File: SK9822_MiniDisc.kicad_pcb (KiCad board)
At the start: 4 copper layers, 220 x 220 mm, 378 parts, among them P1 CONN_01X04, P2 CONN_01X04

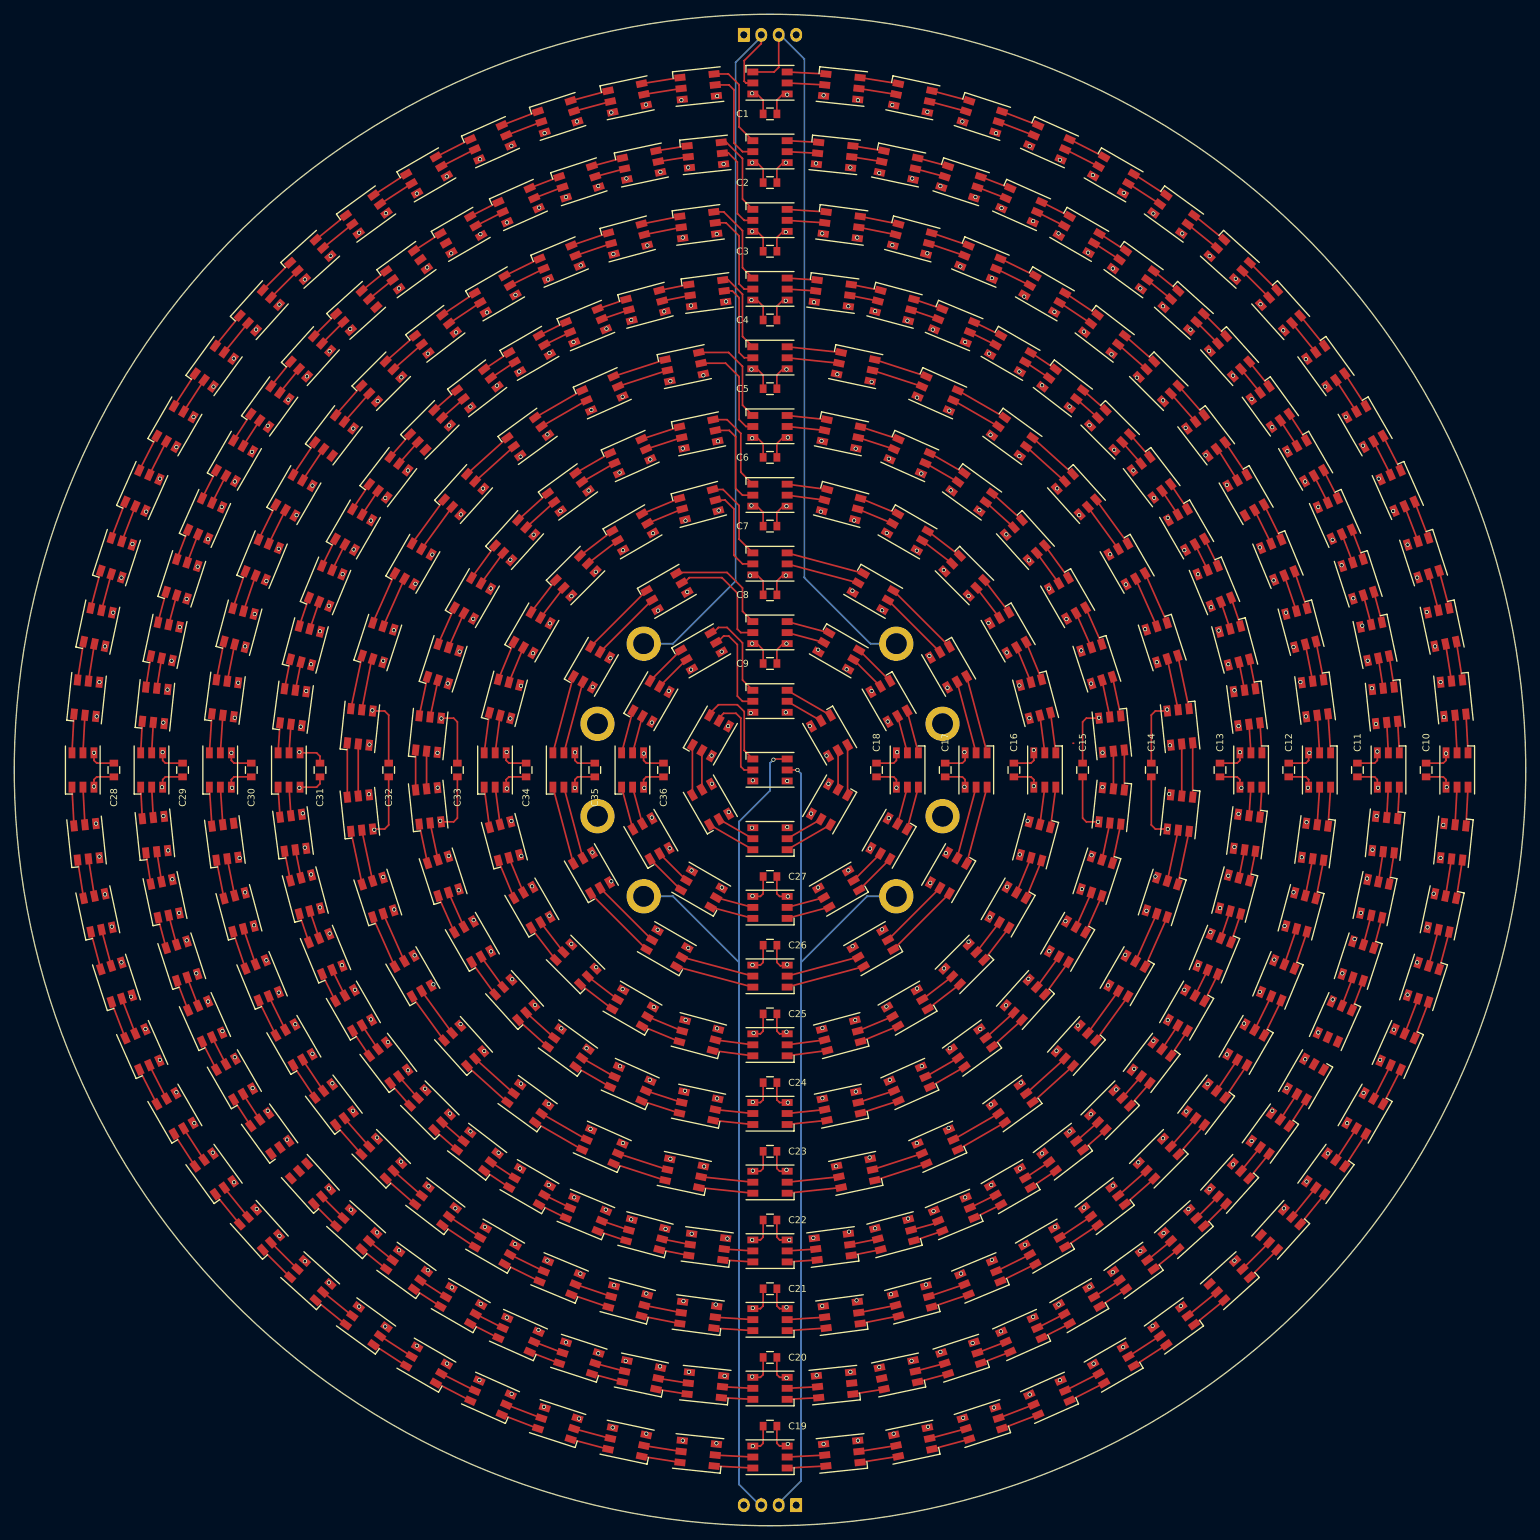
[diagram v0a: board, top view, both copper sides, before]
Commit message: fixing unconnected
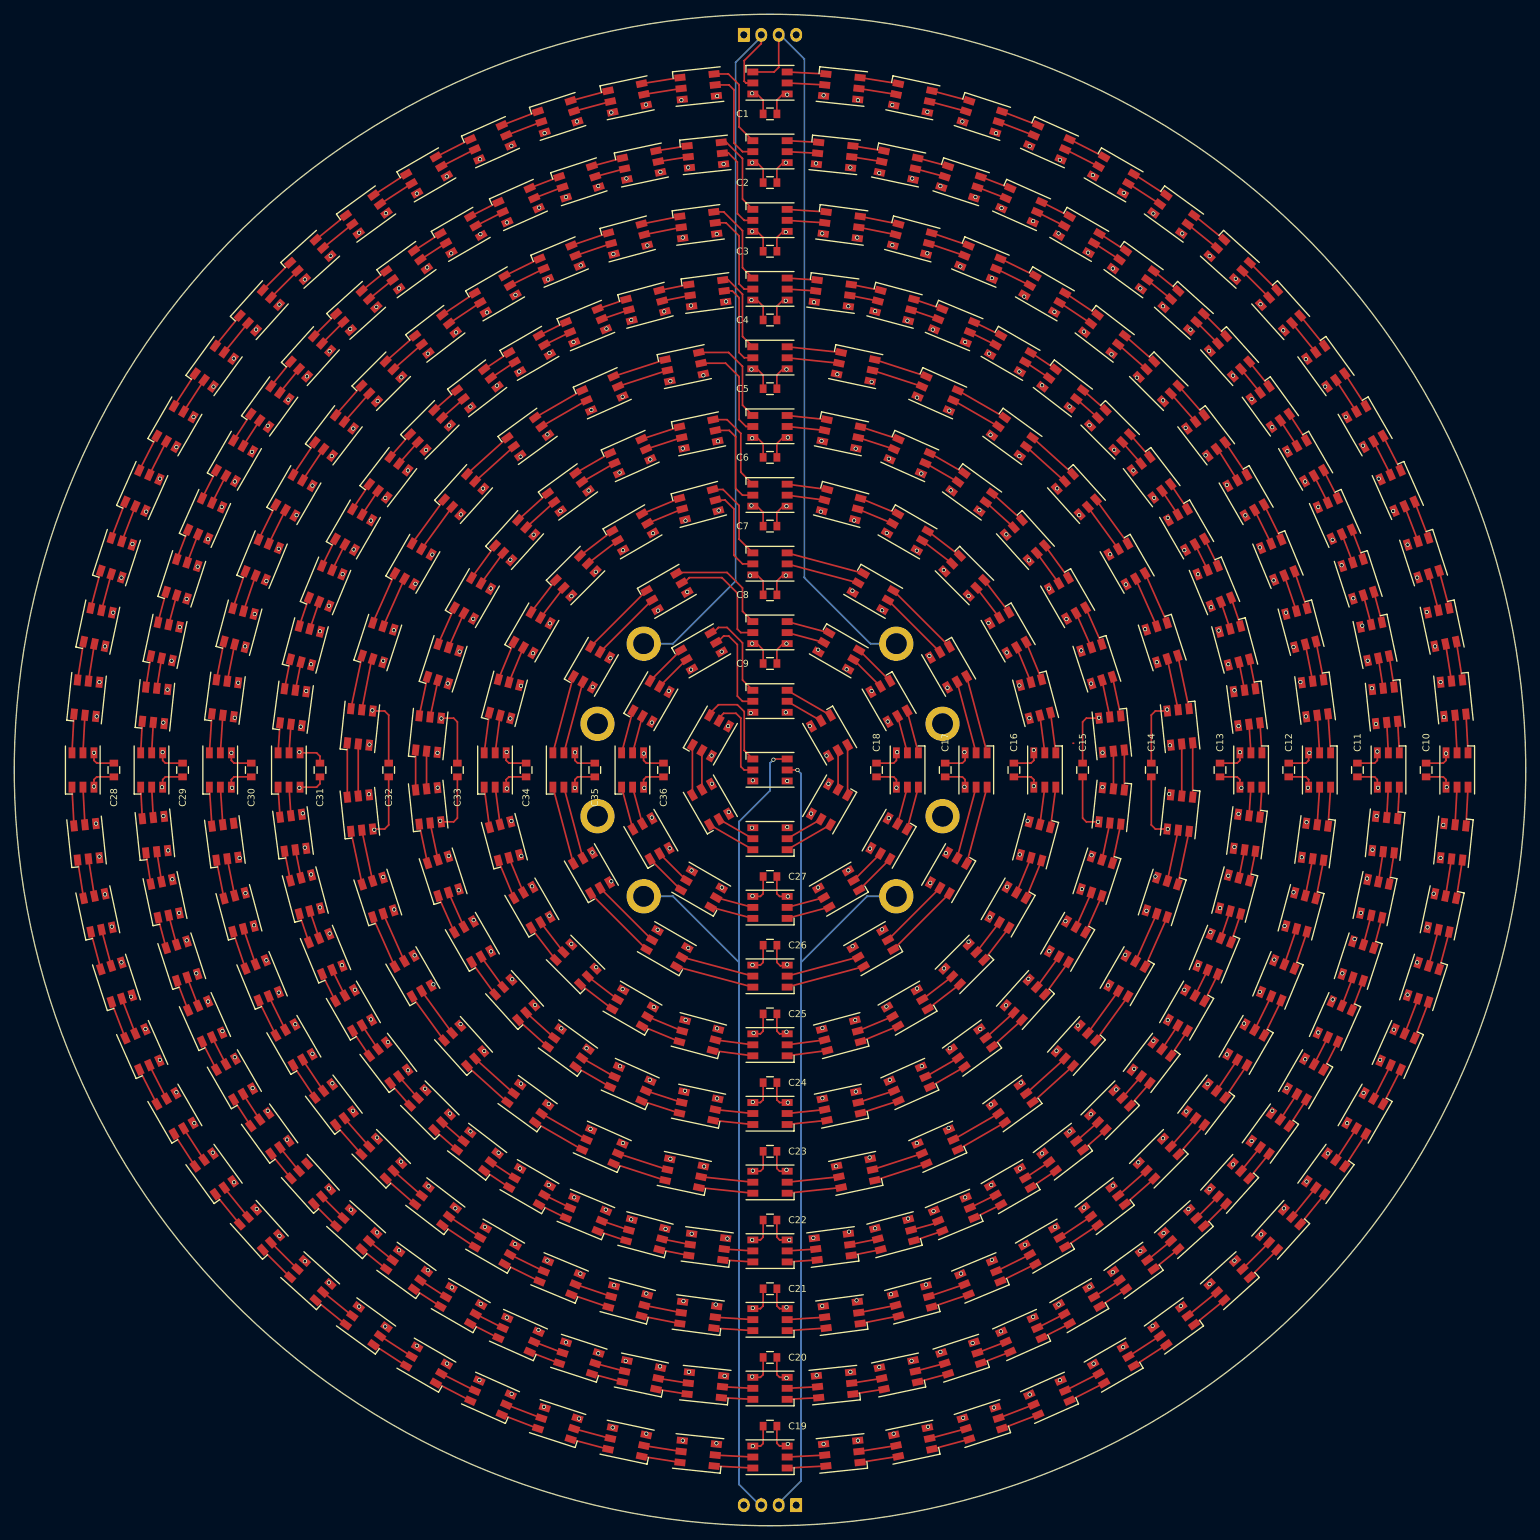
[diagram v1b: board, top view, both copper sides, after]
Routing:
- net VCC: track 4185.0 -> 4203.2 mm, vias 326 -> 330
- net Net-(D100-Pad1): track 0.00 -> 4.59 mm
- net Net-(D80-Pad6): track 0.00 -> 4.59 mm
- net Net-(D115-Pad5): track 0.00 -> 4.43 mm
- net Net-(D100-Pad2): track 0.00 -> 4.43 mm
- net Net-(D89-Pad5): track 0.00 -> 4.43 mm
- net Net-(D80-Pad5): track 0.00 -> 4.43 mm
- net GND: track 4218.6 -> 4218.5 mm, vias 329 -> 331
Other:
- board text added: "CLK_IN"
- board text added: "CLK_OUT"
- board text added: "DAT_IN"
- board text added: "DAT_OUT"
- board text added: "INPUT"
- board text added: "OUTPUT"

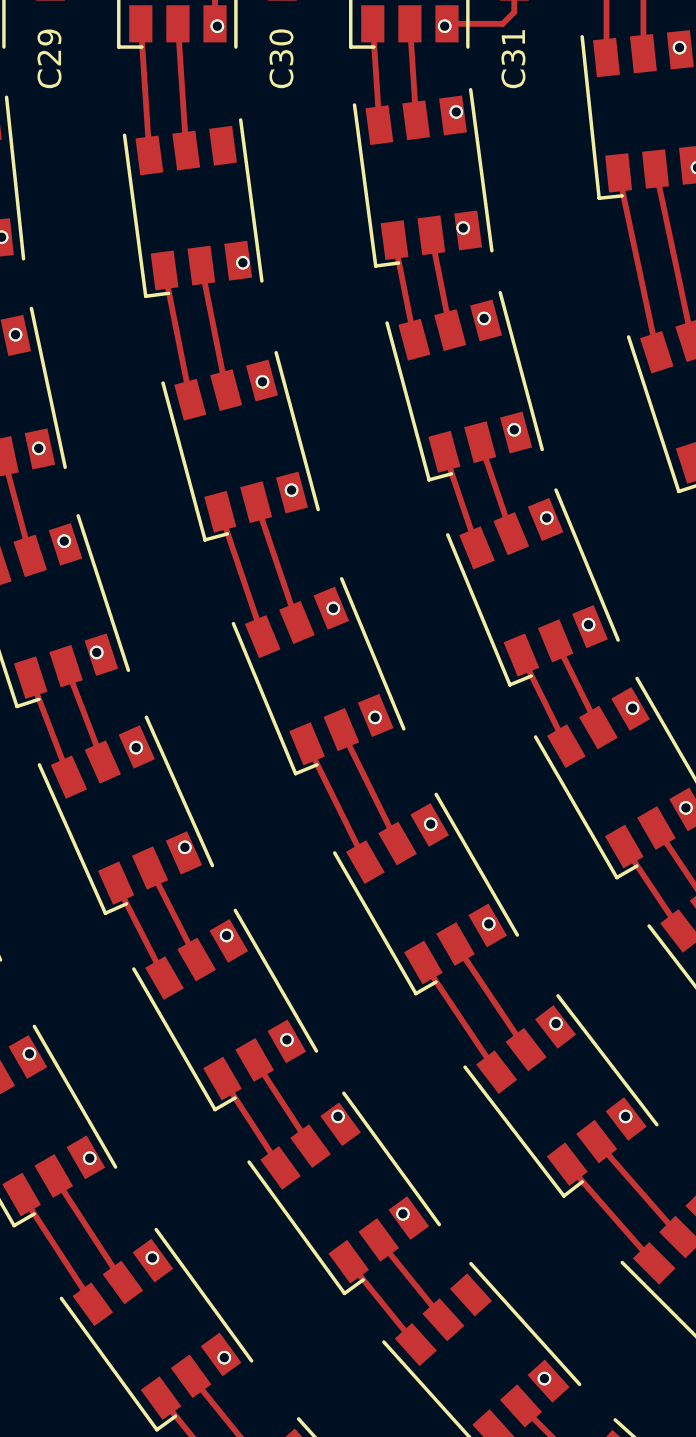
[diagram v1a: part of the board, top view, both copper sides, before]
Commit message: Added vias to D99 and D156 VCC
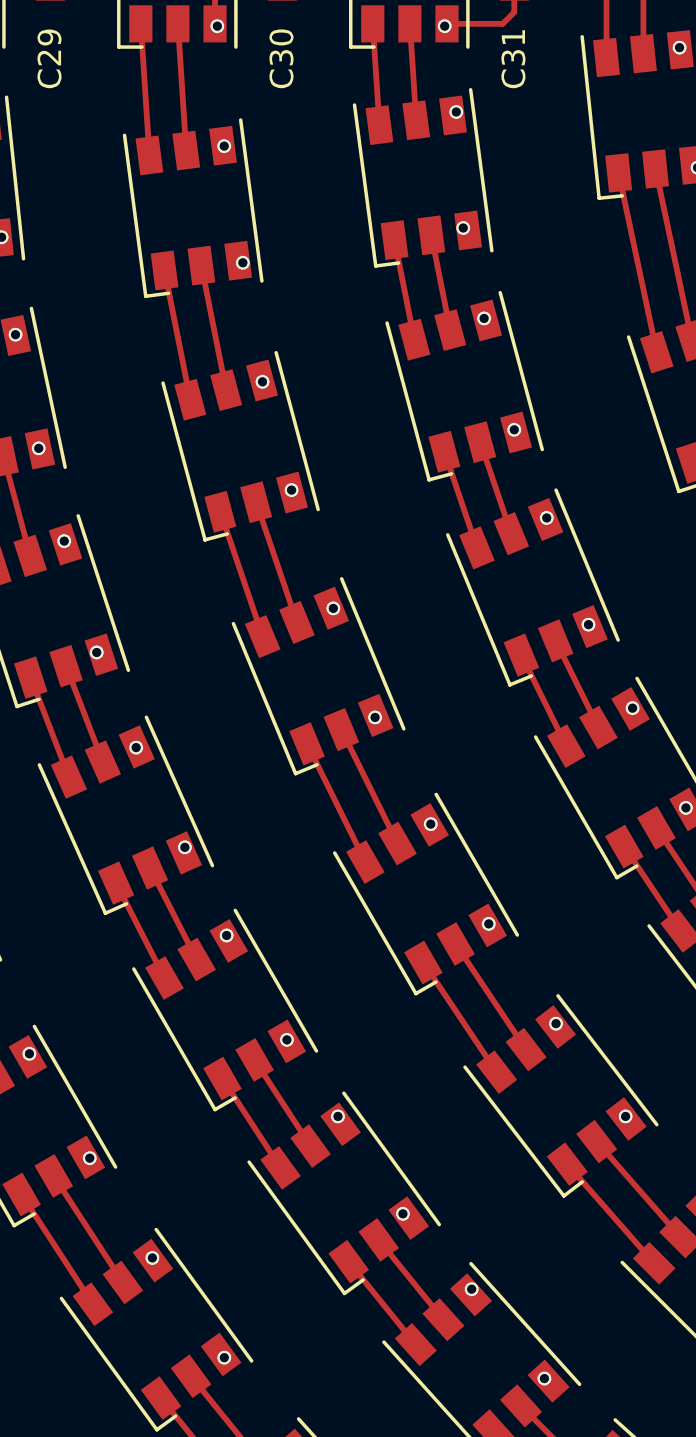
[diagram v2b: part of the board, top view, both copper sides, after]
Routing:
- net VCC: track 4203.2 -> 4214.4 mm, vias 330 -> 332

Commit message: Fixed unconnected again
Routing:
- net GND: track 4218.5 -> 4336.2 mm
- net VCC: track 4214.4 -> 4332.0 mm

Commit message: adding more logos
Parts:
- added G***: OSHW-logo_silkscreen-front_20mm, OSHW-logo:OSHW-logo_silkscreen-front_20mm, B.Cu at (390.0, 197.5)
- added G***: LOGO, Logos:osh_park, B.Cu at (230.0, 197.5)
